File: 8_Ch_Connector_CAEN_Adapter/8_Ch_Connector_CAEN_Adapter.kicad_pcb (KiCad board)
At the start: 2 copper layers, 70 x 60 mm, 9 parts

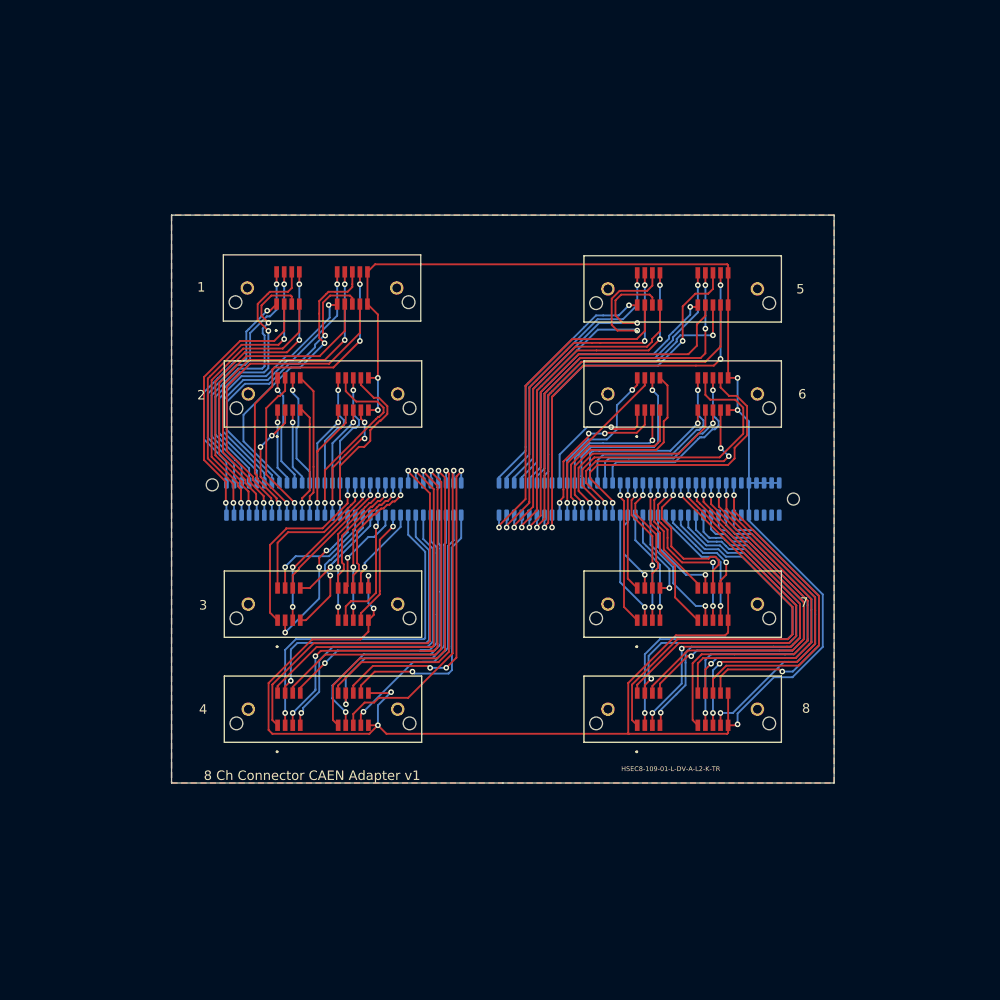
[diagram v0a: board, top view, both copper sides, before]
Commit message: Updated PCBs to include temp sensors
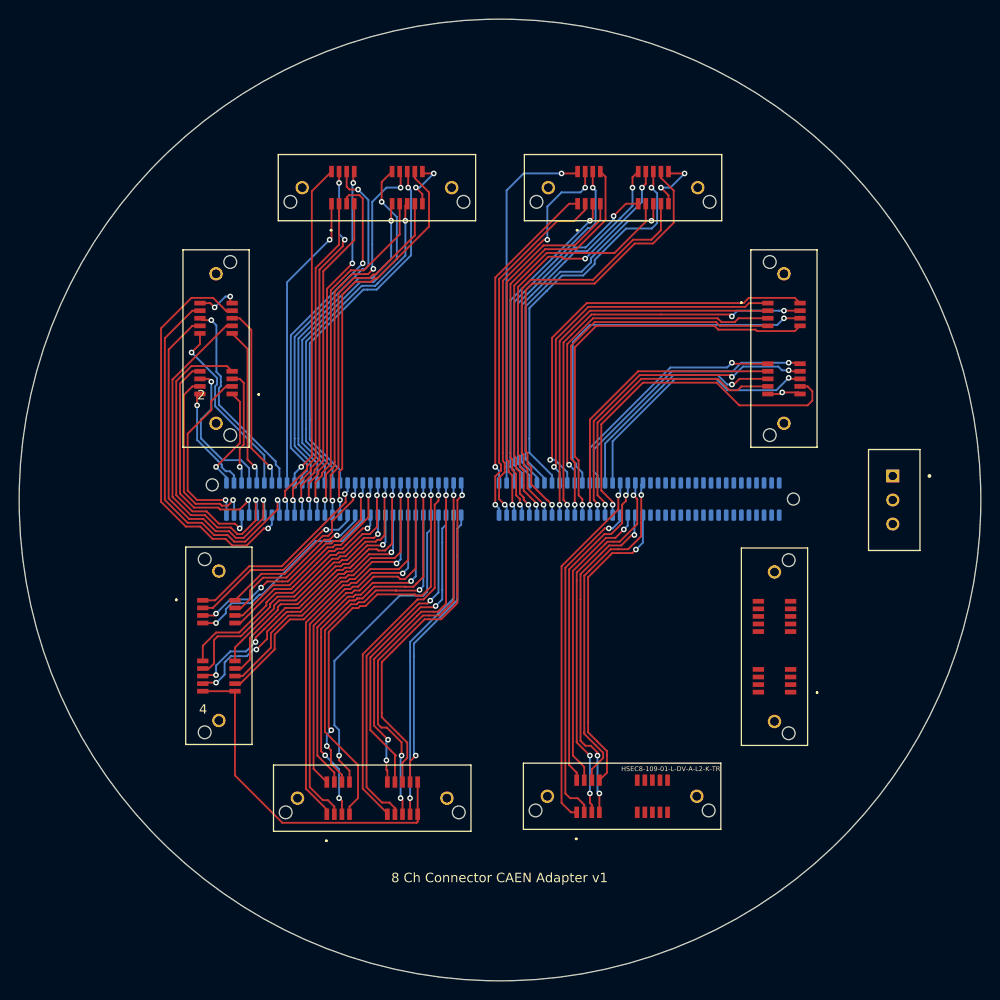
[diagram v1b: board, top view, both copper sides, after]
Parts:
- added REF**: TE_103414-1, AMPMODU:TE_103414-1, F.Cu at (204.5, 85.0)
- moved J** 22.5 mm to (150.0, 52.0)
- moved J** 21.3 mm to (175.9, 116.3)
- moved J** 12.9 mm to (133.0, 69.0), turned to 90 degrees
- moved J** 12.4 mm to (176.0, 52.0)
- moved J** 11.8 mm to (133.3, 100.4), turned to -90 degrees
- moved J** 11.7 mm to (192.0, 100.5), turned to 90 degrees
- moved J** 11.7 mm to (193.0, 69.0), turned to -90 degrees
- moved J** 10.7 mm to (149.5, 116.5)
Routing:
- net GND: track 228.4 -> 58.8 mm, vias 9 -> 7
- net A56: track 44.6 -> 0.00 mm, vias 1 -> 0
- net A57: track 43.3 -> 0.00 mm, vias 1 -> 0
- net A58: track 43.3 -> 0.00 mm, vias 3 -> 0
- net A59: track 40.9 -> 0.00 mm, vias 1 -> 0
- net A60: track 40.8 -> 0.00 mm, vias 1 -> 0
- net K56: track 40.7 -> 0.00 mm, vias 1 -> 0
- net K57: track 40.1 -> 0.00 mm, vias 1 -> 0
- net K58: track 39.7 -> 0.00 mm, vias 1 -> 0
- net A62: track 38.6 -> 0.00 mm, vias 3 -> 0
- net A61: track 37.6 -> 0.00 mm, vias 1 -> 0
- net K59: track 37.5 -> 0.00 mm, vias 1 -> 0
- net K60: track 36.9 -> 0.00 mm, vias 1 -> 0
- net K62: track 35.1 -> 0.00 mm, vias 1 -> 0
- net K61: track 33.7 -> 0.00 mm, vias 1 -> 0
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- removed copper zone on B.Cu, net (none)
- removed copper zone on F.Cu, net (none)
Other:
- board size 70 x 60 mm -> 101.6 x 101.6 mm
- board text removed: "1"
- board text removed: "3"
- board text removed: "5"
- board text removed: "6"
- board text removed: "7"
- board text removed: "8"

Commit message: Finished CAEN adapter
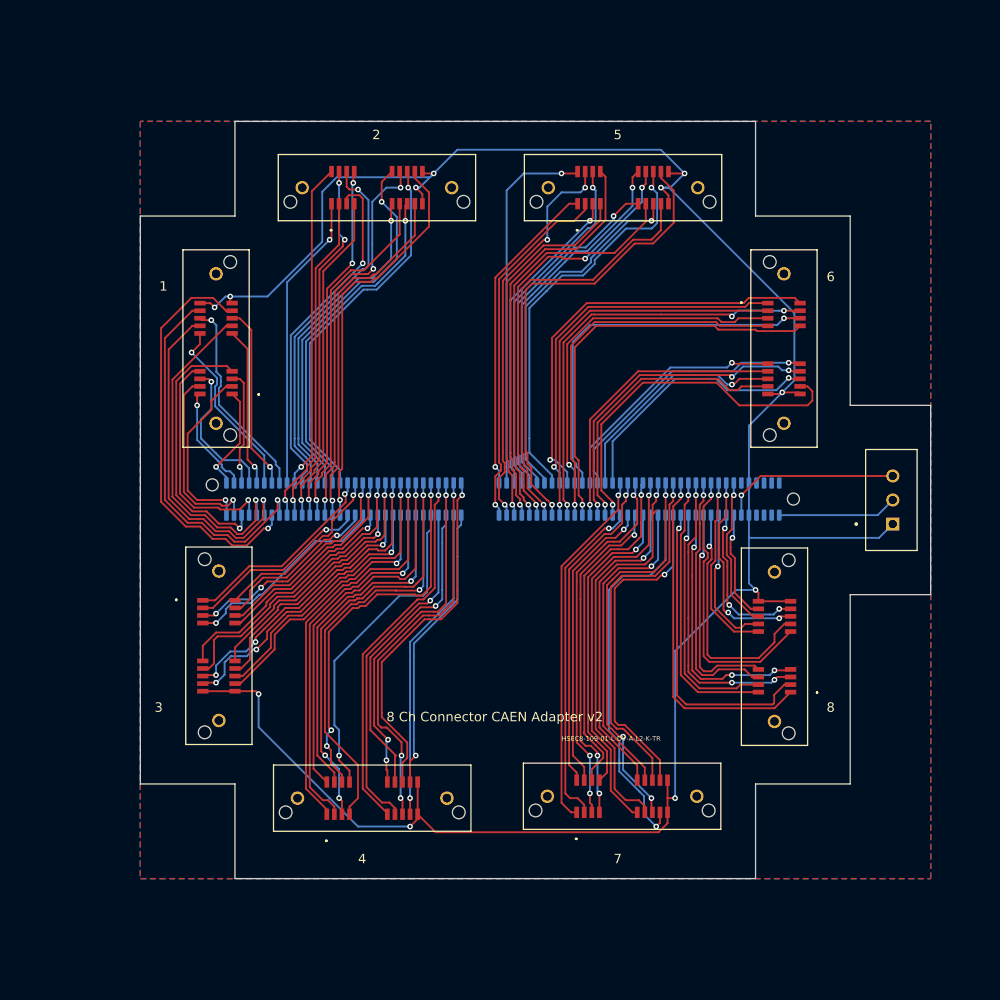
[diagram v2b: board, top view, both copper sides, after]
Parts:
- turned REF** to 90 degrees
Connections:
- REF** pad 1: (no net) -> GND
- REF** pad 2: (no net) -> T_OUT
- REF** pad 3: (no net) -> 3.3V
- REF** pad 130: (no net) -> 3.3V
- REF** pad 140: (no net) -> T_OUT
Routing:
- net GND: track 58.8 -> 245.6 mm, vias 7 -> 11
- net A54: track 0.00 -> 41.7 mm, vias 0 -> 3
- net A52: track 0.00 -> 41.1 mm, vias 0 -> 1
- net A55: track 0.00 -> 40.8 mm, vias 0 -> 1
- net K54: track 0.00 -> 38.4 mm, vias 0 -> 1
- net A53: track 0.00 -> 38.3 mm, vias 0 -> 1
- net K52: track 0.00 -> 37.9 mm, vias 0 -> 1
- net A56: track 0.00 -> 36.5 mm, vias 0 -> 1
- net K55: track 0.00 -> 35.2 mm, vias 0 -> 1
- net K53: track 0.00 -> 34.1 mm, vias 0 -> 1
- net A57: track 0.00 -> 33.0 mm, vias 0 -> 1
- net A58: track 0.00 -> 31.8 mm, vias 0 -> 3
- net A60: track 0.00 -> 29.8 mm, vias 0 -> 1
- net K56: track 0.00 -> 29.6 mm, vias 0 -> 1
- net A59: track 0.00 -> 27.7 mm, vias 0 -> 3
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- added copper zone on B.Cu, net (none)
- added copper zone on F.Cu, net (none)
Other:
- board size 101.6 x 101.6 mm -> 83.5 x 80 mm
- board text added: "1"
- board text added: "3"
- board text added: "5"
- board text added: "6"
- board text added: "7"
- board text added: "8"
- board text added: "8 Ch Connector CAEN Adapter v2"
- board text removed: "8 Ch Connector CAEN Adapter v1"

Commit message: Updated boards with connector HSEC8-109-01-L-DV-A-BL
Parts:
- removed J** (x8): HSEC810901LDVAL2KTR, KiCad:HSEC810901LDVAL2KTR
- added REF**: Samtec_HSEC8-109-01-X-DV-A-BL_2x09_P0.8mm_Pol04_Socket_Weld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, Connector_Samtec_HSEC8:Samtec_HSEC8-109-01-X-DV-A-BL_2x09_P0.8mm_Pol04_Socket_WeldTabs_BoardLocks, F.Cu at (175.9, 51.3)
- added REF**: Samtec_HSEC8-109-01-X-DV-A-BL_2x09_P0.8mm_Pol04_Socket_Weld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, Connector_Samtec_HSEC8:Samtec_HSEC8-109-01-X-DV-A-BL_2x09_P0.8mm_Pol04_Socket_WeldTabs_BoardLocks, F.Cu at (148.3, 119.0)
- added REF**: Samtec_HSEC8-109-01-X-DV-A-BL_2x09_P0.8mm_Pol04_Socket_Weld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, Connector_Samtec_HSEC8:Samtec_HSEC8-109-01-X-DV-A-BL_2x09_P0.8mm_Pol04_Socket_WeldTabs_BoardLocks, F.Cu at (132.8, 69.1)
- added REF**: Samtec_HSEC8-109-01-X-DV-A-BL_2x09_P0.8mm_Pol04_Socket_Weld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, Connector_Samtec_HSEC8:Samtec_HSEC8-109-01-X-DV-A-BL_2x09_P0.8mm_Pol04_Socket_WeldTabs_BoardLocks, F.Cu at (133.0, 100.4)
- added REF**: Samtec_HSEC8-109-01-X-DV-A-BL_2x09_P0.8mm_Pol04_Socket_Weld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, Connector_Samtec_HSEC8:Samtec_HSEC8-109-01-X-DV-A-BL_2x09_P0.8mm_Pol04_Socket_WeldTabs_BoardLocks, F.Cu at (176.0, 119.0)
- added REF**: Samtec_HSEC8-109-01-X-DV-A-BL_2x09_P0.8mm_Pol04_Socket_Weld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, Connector_Samtec_HSEC8:Samtec_HSEC8-109-01-X-DV-A-BL_2x09_P0.8mm_Pol04_Socket_WeldTabs_BoardLocks, F.Cu at (192.8, 69.0)
- added REF**: Samtec_HSEC8-109-01-X-DV-A-BL_2x09_P0.8mm_Pol04_Socket_Weld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, Connector_Samtec_HSEC8:Samtec_HSEC8-109-01-X-DV-A-BL_2x09_P0.8mm_Pol04_Socket_WeldTabs_BoardLocks, F.Cu at (148.6, 51.3)
- added REF**: Samtec_HSEC8-109-01-X-DV-A-BL_2x09_P0.8mm_Pol04_Socket_Weld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, Connector_Samtec_HSEC8:Samtec_HSEC8-109-01-X-DV-A-BL_2x09_P0.8mm_Pol04_Socket_WeldTabs_BoardLocks, F.Cu at (192.3, 100.6)
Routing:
- net GND: track 245.6 -> 191.5 mm, vias 11 -> 10
- net K29: track 33.5 -> 37.7 mm
- net A31: track 33.5 -> 37.3 mm
- net A54: track 41.7 -> 45.4 mm
- net K31: track 30.6 -> 33.6 mm
- net A52: track 41.1 -> 44.0 mm
- net A53: track 38.3 -> 41.3 mm
- net A49: track 35.6 -> 38.3 mm
- net A50: track 39.1 -> 41.9 mm
- net K52: track 37.9 -> 40.7 mm
- net K49: track 31.5 -> 34.2 mm
- net K48: track 34.7 -> 37.5 mm
- net K53: track 34.1 -> 36.9 mm
- net A48: track 38.4 -> 41.1 mm
- net A51: track 35.9 -> 38.4 mm
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- added copper zone on B.Cu, net GND
- added copper zone on F.Cu, net GND
- removed copper zone on B.Cu, net (none)
- removed copper zone on F.Cu, net (none)
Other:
- outline, holes or cut-outs redrawn
- board text added: "HSEC8-109-01-L-DV-A-BL"
- board text removed: "8 Ch Connector CAEN Adapter v2"
- board text removed: "HSEC8-109-01-L-DV-A-L2-K-TR"
